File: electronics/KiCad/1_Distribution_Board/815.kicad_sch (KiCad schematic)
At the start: 41 parts, among them J12 Conn_01x06, J13 Conn_01x10, J17 Conn_02x08_Odd_Even, U6 PCA9306, U7 PCA9685PW, Y1 25MHz

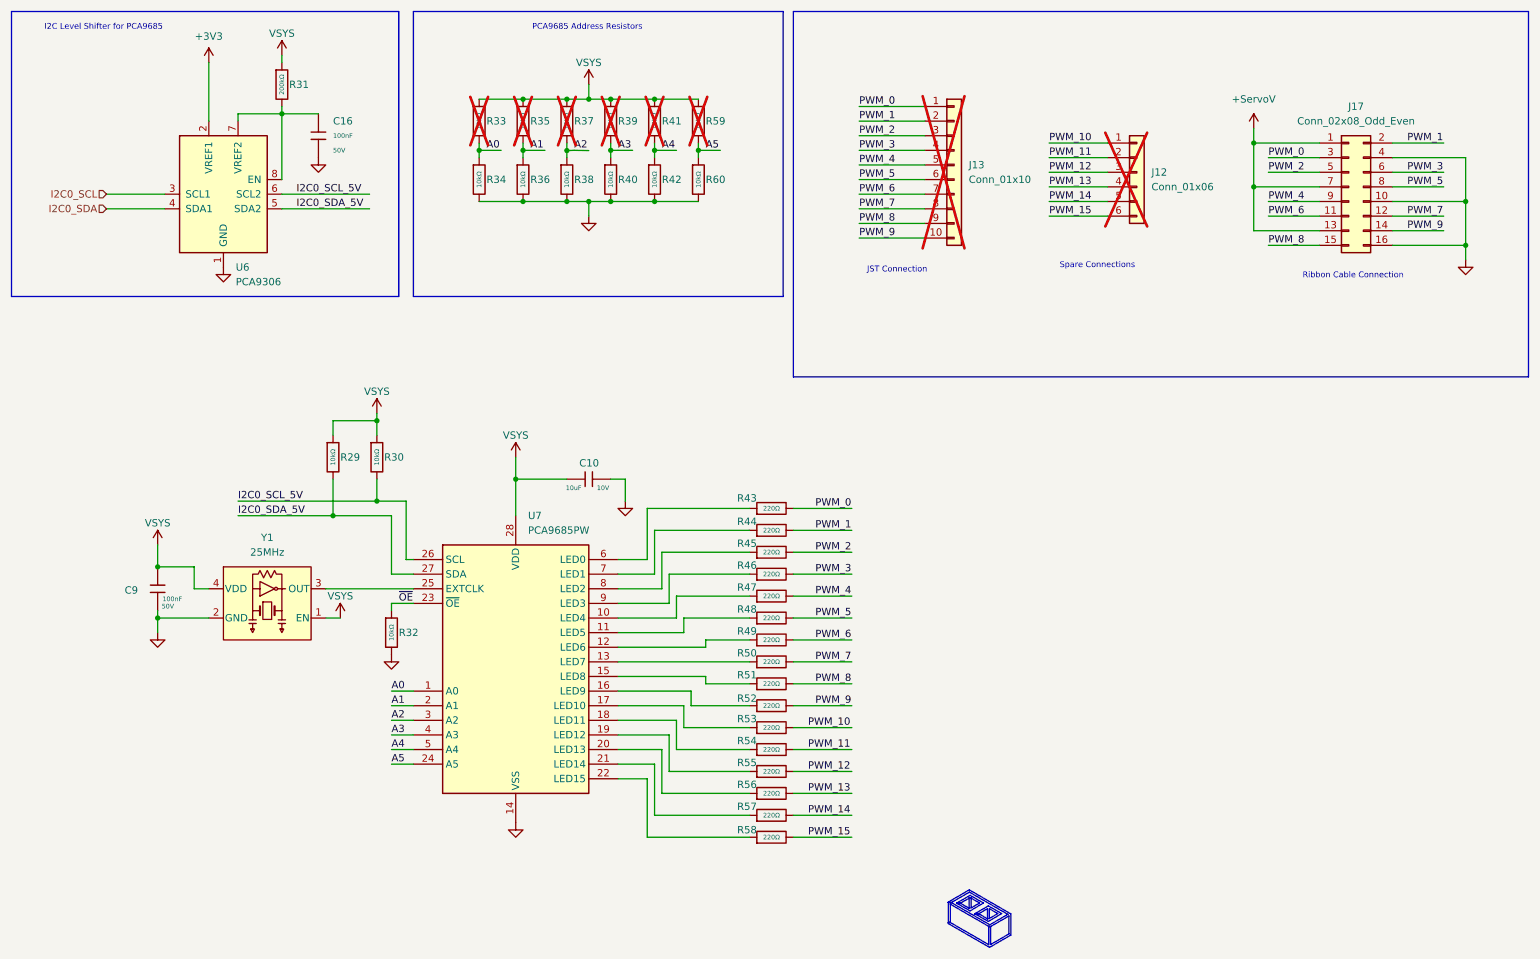
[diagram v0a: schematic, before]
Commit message: Update to board with pull up/down resistors, clean up.
Updated with pull up and down resistors. Corrected some layout. Removed unused parts.

Still need to clean up some layout issues and reduce the circuit down to only what is needed.
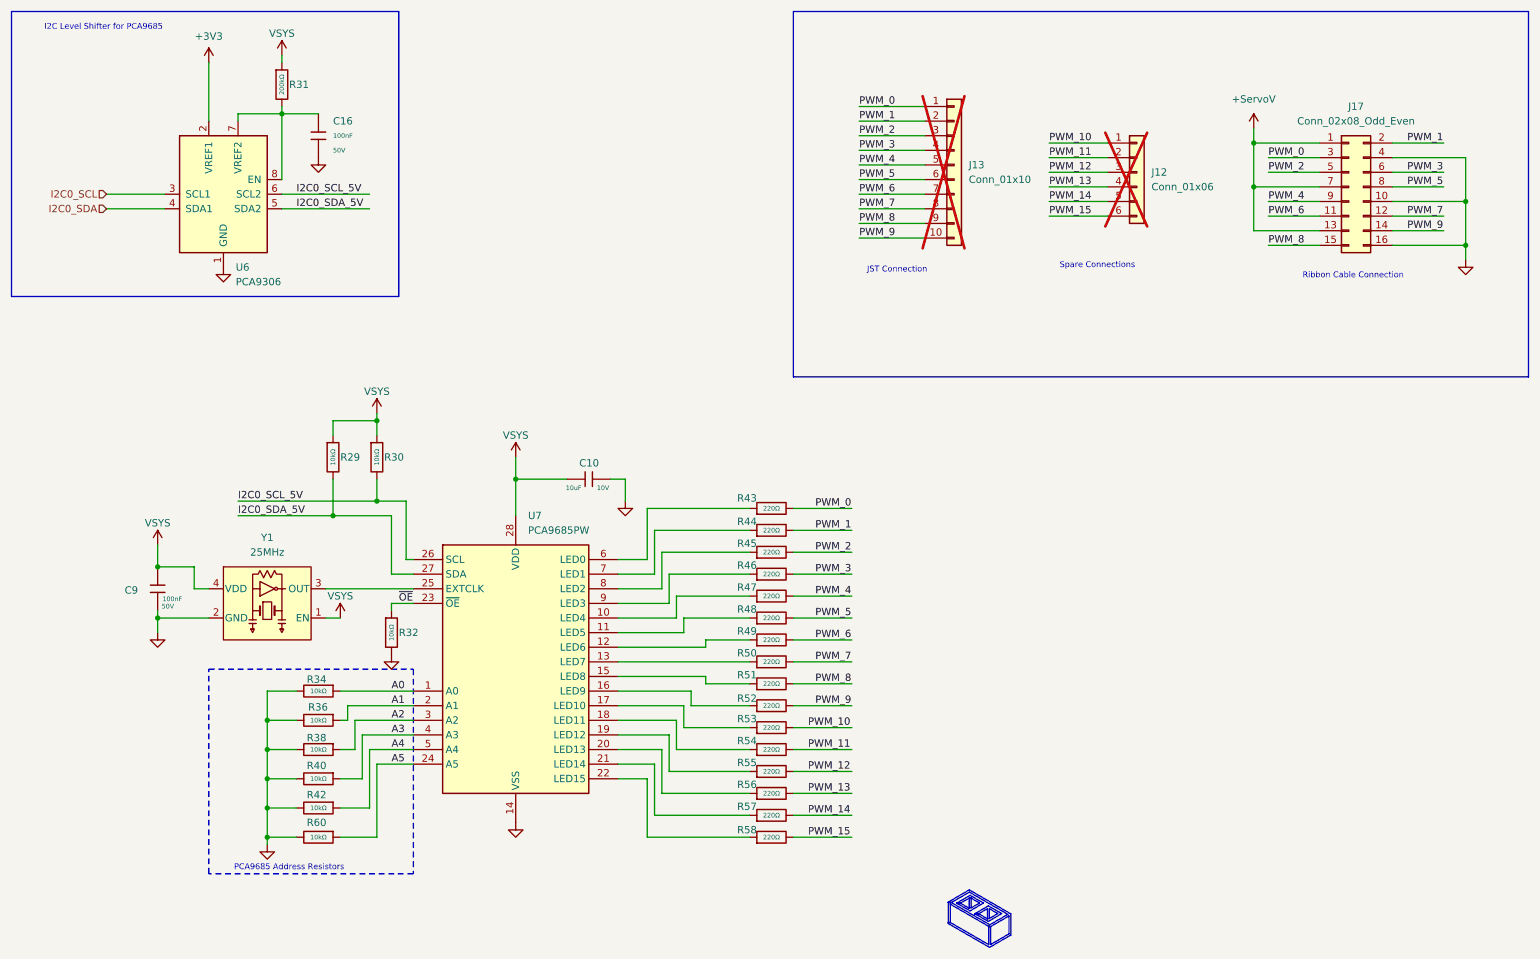
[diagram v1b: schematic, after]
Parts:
- removed R33, R35, R37, R39, R41, R59: 10kΩ, PCM_JLCPCB:R_0603, symbol PCM_JLCPCB-Resistors:0603,10kΩ
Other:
- moved on the sheet: R34, R36, R38, R40, R42, R60
